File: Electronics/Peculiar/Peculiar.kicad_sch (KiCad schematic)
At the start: 13 parts, among them U5 ${SIM.PARAMS}, U6 ${SIM.PARAMS}

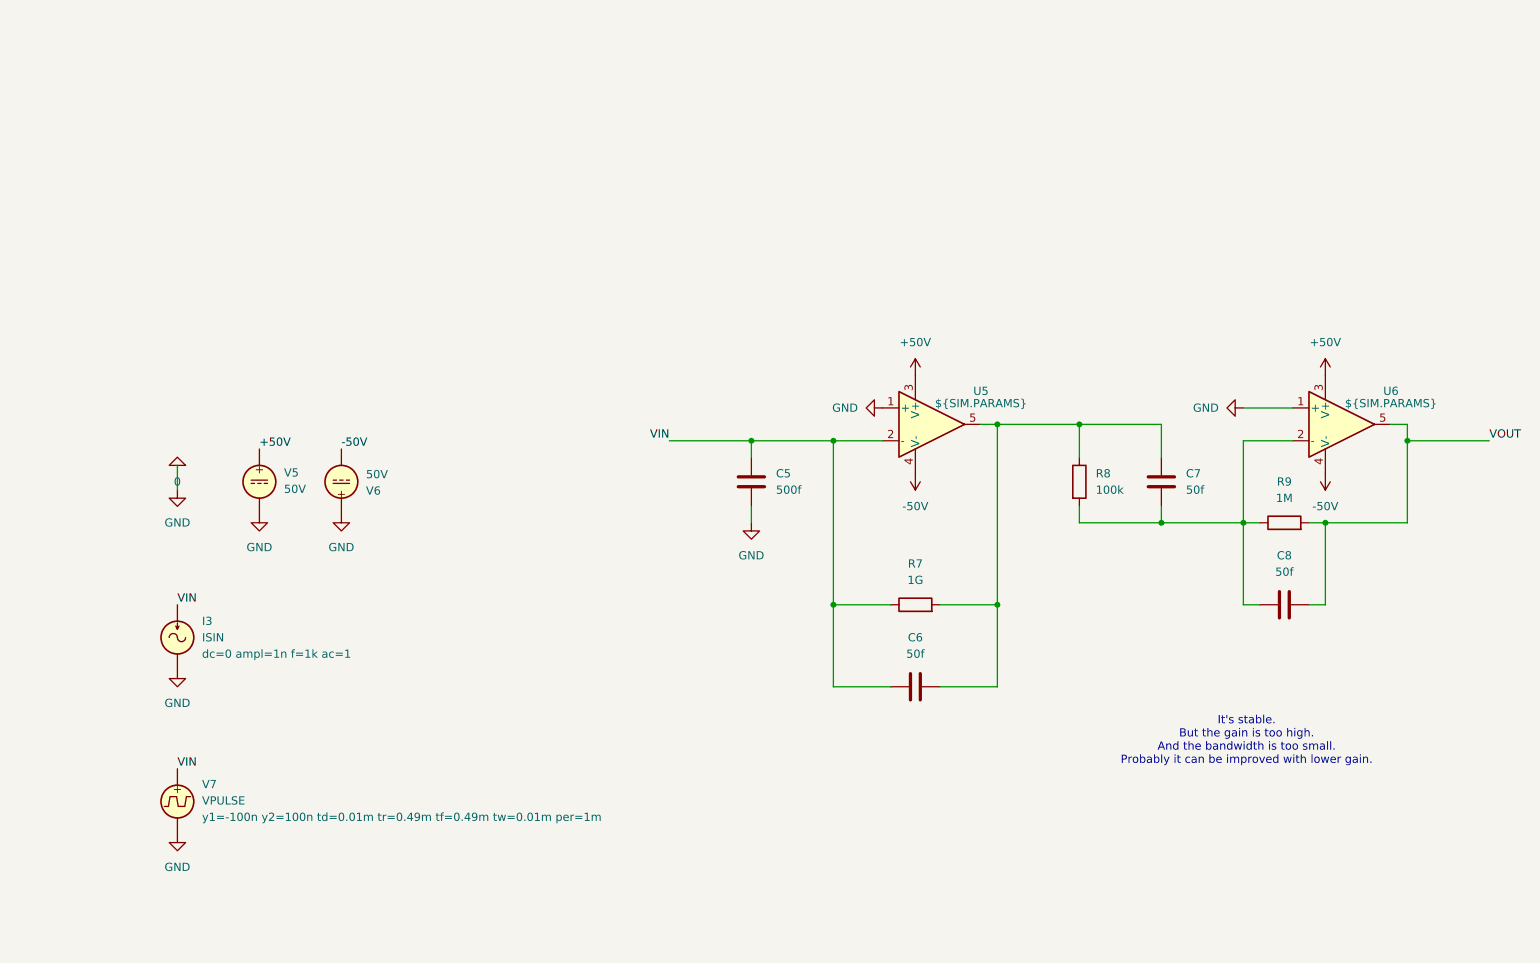
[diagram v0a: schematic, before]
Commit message: Implement the peculiar equivalent schematics from OPA380
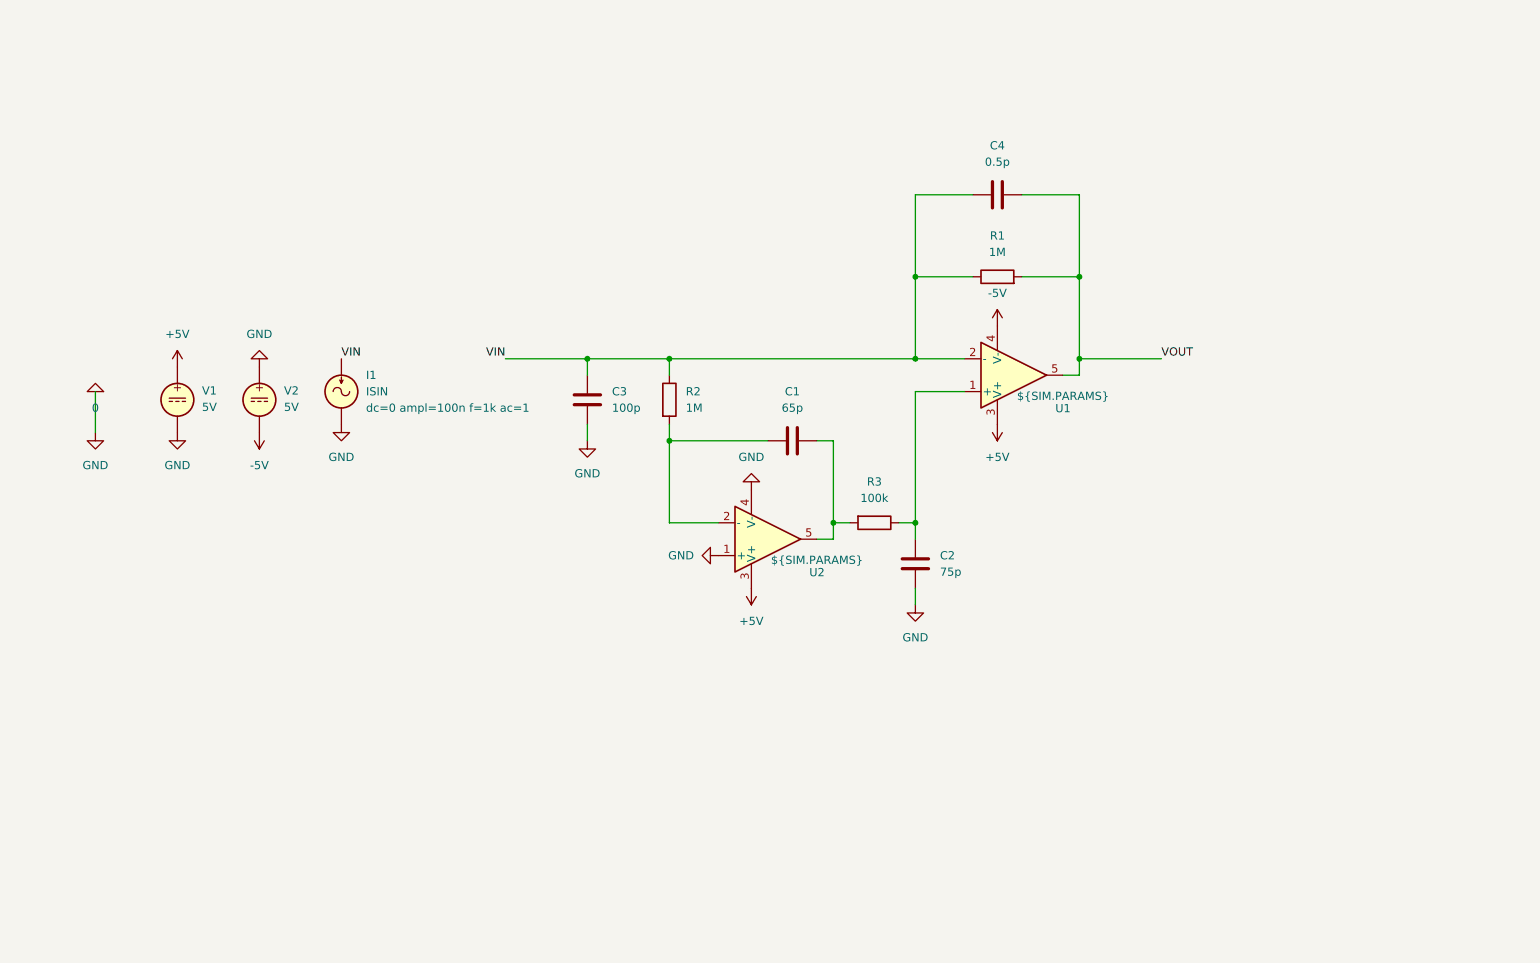
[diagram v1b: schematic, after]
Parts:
- removed C5: 500f, symbol Device:C
- removed C6, C7, C8: 50f, symbol Device:C
- removed I3: ISIN, symbol Simulation_SPICE:ISIN
- removed R7: 1G, symbol Device:R
- removed R8: 100k, symbol Device:R
- removed R9: 1M, symbol Device:R
- removed U5, U6: ${SIM.PARAMS}, symbol Simulation_SPICE:OPAMP
- removed V5, V6: 50V, symbol Simulation_SPICE:VDC
- removed V7: VPULSE, symbol Simulation_SPICE:VPULSE
- added C1: 65p, symbol Device:C
- added C2: 75p, symbol Device:C
- added C3: 100p, symbol Device:C
- added C4: 0.5p, symbol Device:C
- added I1: ISIN, symbol Simulation_SPICE:ISIN
- added R1, R2: 1M, symbol Device:R
- added R3: 100k, symbol Device:R
- added U1, U2: ${SIM.PARAMS}, symbol Simulation_SPICE:OPAMP
- added V1, V2: 5V, symbol Simulation_SPICE:VDC
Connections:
- net 0: now also C2.1, C3.1, I1.2, U2.1 (+), U2.4 (V-), V1.2, V2.1
- net VIN: now also C3.2, C4.1, I1.1, R1.1, R2.1, U1.2 (-)
- net VOUT: now also C4.2, R1.2, U1.5
- new net: C2.2, R3.1, U1.1 (+)
- new net: C1.1, R2.2, U2.2 (-)
- new net: C1.2, R3.2, U2.5
- new net +5V: U1.3 (V+), U2.3 (V+), V1.1
- new net -5V: U1.4 (V-), V2.2
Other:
- note removed: "It's stable.r But the gain is too high. And the bandwidth is too small. Probably it can be improved with lower gain."

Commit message: Create the peculiar transimpedance amplifier
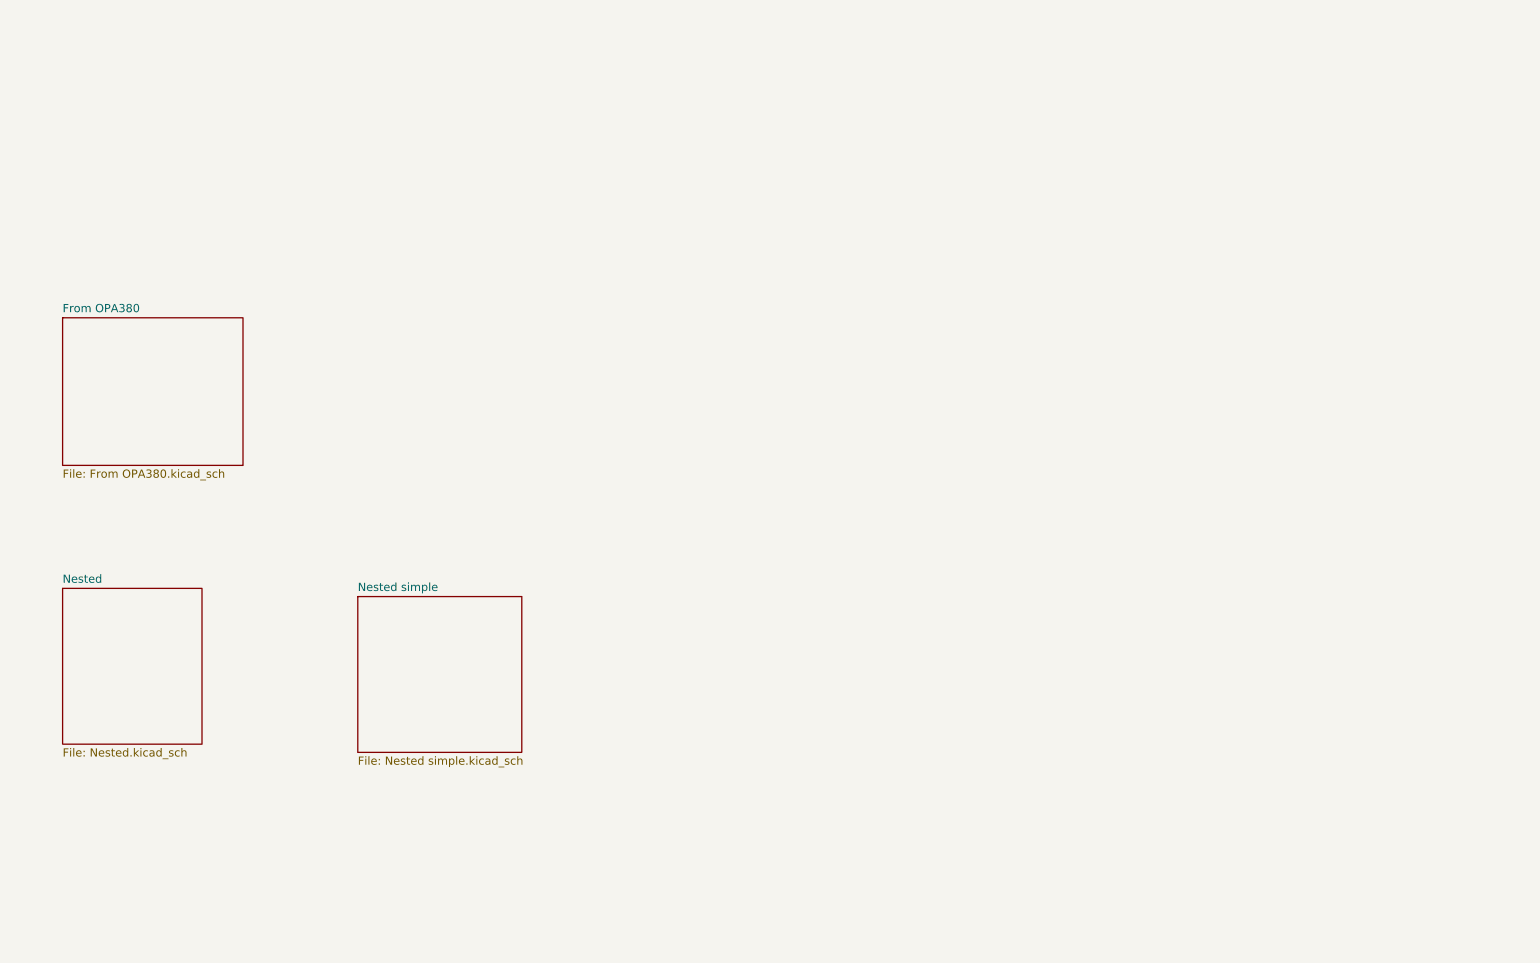
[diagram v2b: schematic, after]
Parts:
- removed C1: 65p, symbol Device:C
- removed C2: 75p, symbol Device:C
- removed C3: 100p, symbol Device:C
- removed C4: 0.5p, symbol Device:C
- removed I1: ISIN, symbol Simulation_SPICE:ISIN
- removed R1, R2: 1M, symbol Device:R
- removed R3: 100k, symbol Device:R
- removed U1, U2: ${SIM.PARAMS}, symbol Simulation_SPICE:OPAMP
- removed V1, V2: 5V, symbol Simulation_SPICE:VDC
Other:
- added sheet From OPA380 (From OPA380.kicad_sch)
- added sheet Nested (Nested.kicad_sch)
- added sheet Nested simple (Nested simple.kicad_sch)

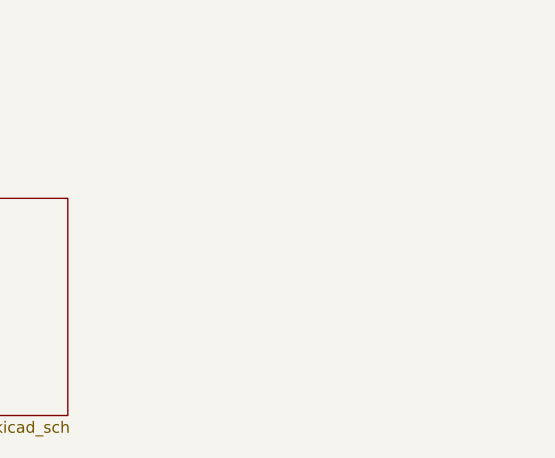
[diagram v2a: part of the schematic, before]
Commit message: Improve the peculiar TIA
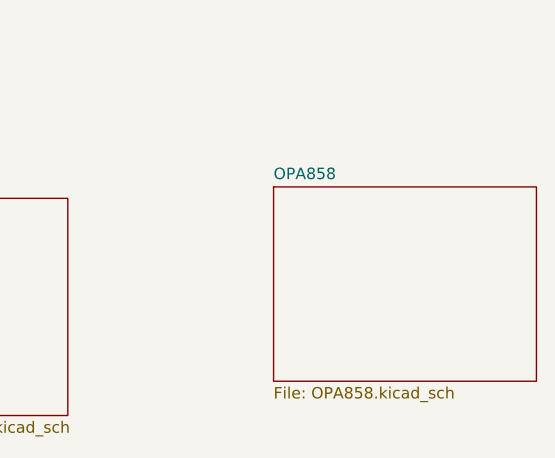
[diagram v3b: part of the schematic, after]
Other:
- added sheet OPA858 (OPA858.kicad_sch)
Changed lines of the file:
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@@
 	(paper "A4")
+	(sheet
+		(at 127 111.76)
+		(size 29.21 21.59)
+		(exclude_from_sim no)
+		(in_bom yes)
+		(on_board yes)
+		(dnp no)
+		(fields_autoplaced yes)
+		(stroke
+			(width 0.1524)
+			(type solid)
+		)
+		(fill
+			(color 0 0 0 0)
+		)
+		(property "Sheetname" "OPA858"
+			(at 127 111.0484 0)
+			(show_name no)
+			(do_not_autoplace no)
+			(effects
+				(font
+					(size 1.27 1.27)
+				)
+				(justify left bottom)
+			)
+		)
+		(property "Sheetfile" "OPA858.kicad_sch"
+			(at 127 133.9346 0)
+			(show_name no)
+			(do_not_autoplace no)
+			(effects
+				(font
+					(size 1.27 1.27)
+				)
+				(justify left top)
+			)
+		)
+		(instances
+			(project "Peculiar"
+				(path "/db27cf5d-1015-467f-a739-ab2eb7f0a1b5"
+					(page "5")
+				)
+			)
+		)
+	)
 	(sheet
 		(at 78.74 113.03)
 		(size 25.4 24.13)
-		(exclude_from_sim no)
+		(exclude_from_sim yes)
 		(in_bom yes)
 		(on_board yes)

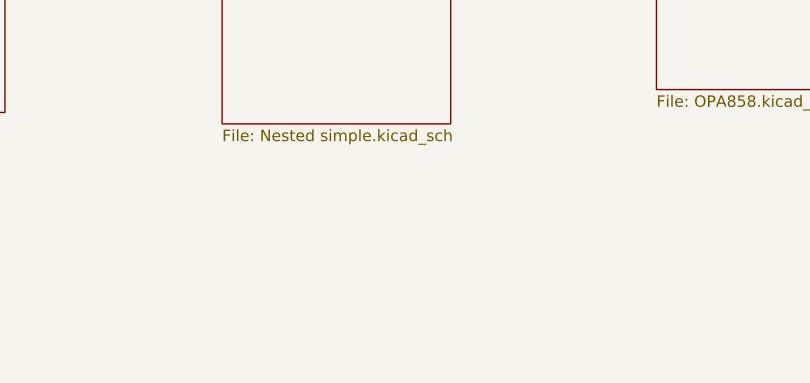
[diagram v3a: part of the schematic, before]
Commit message: Add LMC606 to simulation
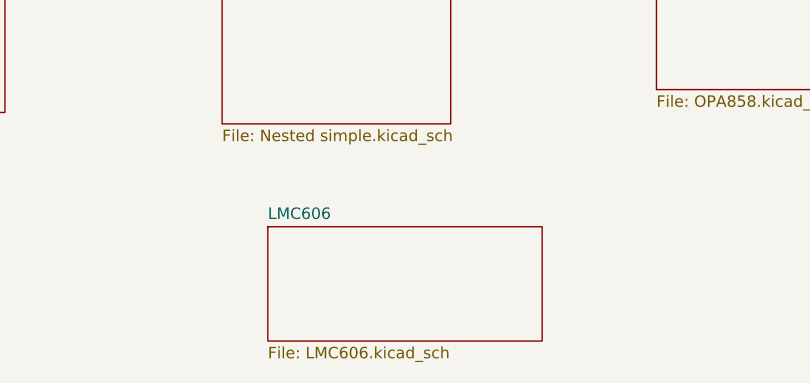
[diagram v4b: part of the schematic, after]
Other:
- added sheet LMC606 (LMC606.kicad_sch)
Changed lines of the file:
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@@
 		(at 127 111.76)
 		(size 29.21 21.59)
-		(exclude_from_sim no)
+		(exclude_from_sim yes)
 		(in_bom yes)
 		(on_board yes)
@@
 				)
 			)
+		)
+	)
+	(sheet
+		(at 83.82 148.59)
+		(size 30.48 12.7)
+		(exclude_from_sim no)
+		(in_bom yes)
+		(on_board yes)
+		(dnp no)
+		(fields_autoplaced yes)
+		(stroke
+			(width 0.1524)
+			(type solid)
+		)
+		(fill
+			(color 0 0 0 0)
+		)
+		(property "Sheetname" "LMC606"
+			(at 83.82 147.8784 0)
+			(show_name no)
+			(do_not_autoplace no)
+			(effects
+				(font
+					(size 1.27 1.27)
+				)
+				(justify left bottom)
+			)
+		)
+		(property "Sheetfile" "LMC606.kicad_sch"
+			(at 83.82 161.8746 0)
+			(show_name no)
+			(do_not_autoplace no)
+			(effects
+				(font
+					(size 1.27 1.27)
+				)
+				(justify left top)
+			)
+		)
+		(instances
+			(project "Peculiar"
+				(path "/db27cf5d-1015-467f-a739-ab2eb7f0a1b5"
+					(page "6")
+				)
+			)

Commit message: Create some other simulations
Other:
- added sheet Three Op Amps (Three Op Amps.kicad_sch)
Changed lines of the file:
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@@
 	(paper "A4")
+	(sheet
+		(at 166.37 143.51)
+		(size 22.86 11.43)
+		(exclude_from_sim yes)
+		(in_bom yes)
+		(on_board yes)
+		(dnp no)
+		(fields_autoplaced yes)
+		(stroke
+			(width 0.1524)
+			(type solid)
+		)
+		(fill
+			(color 0 0 0 0)
+		)
+		(property "Sheetname" "Three Op Amps"
+			(at 166.37 142.7984 0)
+			(show_name no)
+			(do_not_autoplace no)
+			(effects
+				(font
+					(size 1.27 1.27)
+				)
+				(justify left bottom)
+			)
+		)
+		(property "Sheetfile" "Three Op Amps.kicad_sch"
+			(at 166.37 155.5246 0)
+			(show_name no)
+			(do_not_autoplace no)
+			(effects
+				(font
+					(size 1.27 1.27)
+				)
+				(justify left top)
+			)
+		)
+		(instances
+			(project "Peculiar"
+				(path "/db27cf5d-1015-467f-a739-ab2eb7f0a1b5"
+					(page "8")
+				)
+			)
+		)
+	)
 	(sheet
 		(at 127 111.76)
 		(size 29.21 21.59)
-		(exclude_from_sim yes)
+		(exclude_from_sim no)
 		(in_bom yes)
 		(on_board yes)
@@
 		(at 83.82 148.59)
 		(size 30.48 12.7)
-		(exclude_from_sim no)
+		(exclude_from_sim yes)
 		(in_bom yes)
 		(on_board yes)
